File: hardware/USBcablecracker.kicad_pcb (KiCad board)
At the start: 2 copper layers, 100 x 50 mm, 57 parts, among them P1 USB_A, P10 USB_A, P11 USB_B, P12 CONN_01X09, P2 CONN_01X02, P3 USB_B-Micro, P6 CONN_01X09, P7 USB_B-Mini, P8 USB_B-Micro-3.0, P9 USB_TYPEC-S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

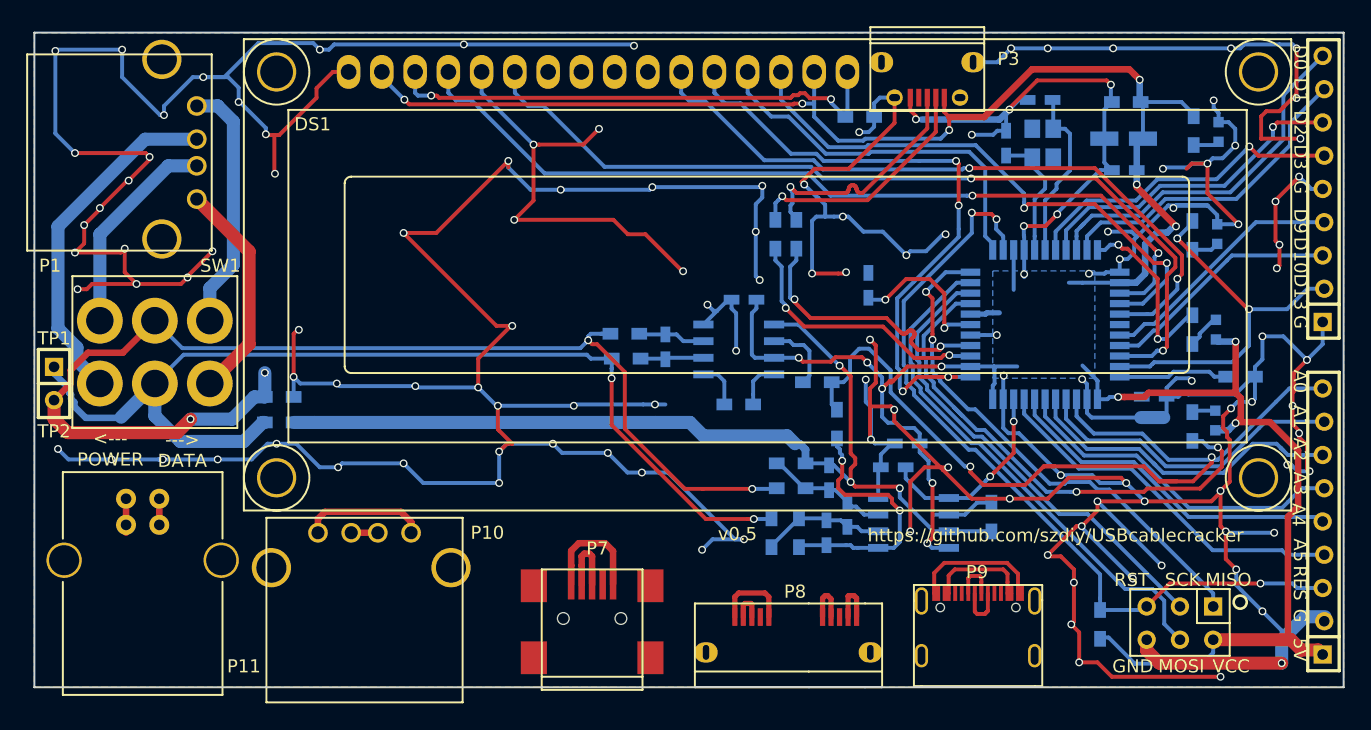
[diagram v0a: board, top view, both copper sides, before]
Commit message: Board cleanup first pass (still need to reconnect GND to U1)
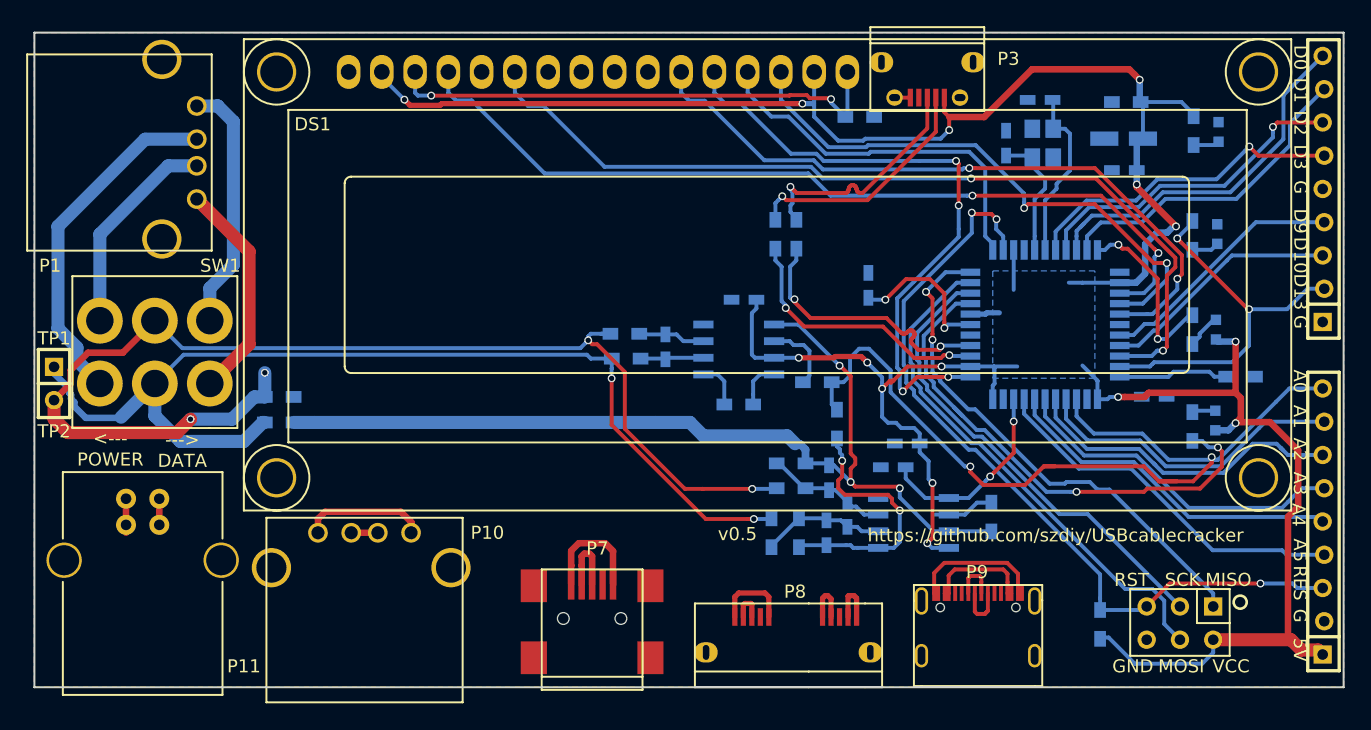
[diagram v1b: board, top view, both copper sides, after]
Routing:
- net GND: track 692.2 -> 1.20 mm, vias 128 -> 0
- net /D7: track 48.2 -> 47.6 mm

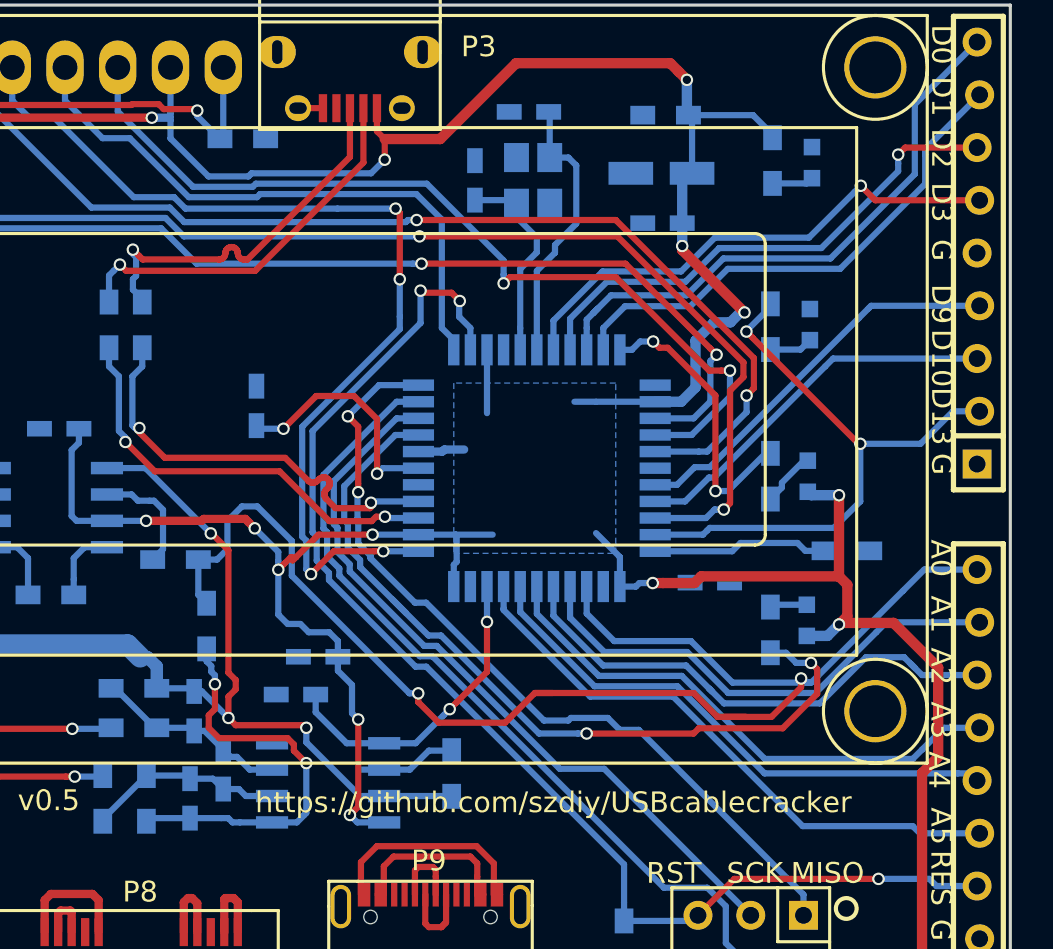
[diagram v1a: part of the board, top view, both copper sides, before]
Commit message: fixes net name (+5C to +5V), big hands -> big led pads
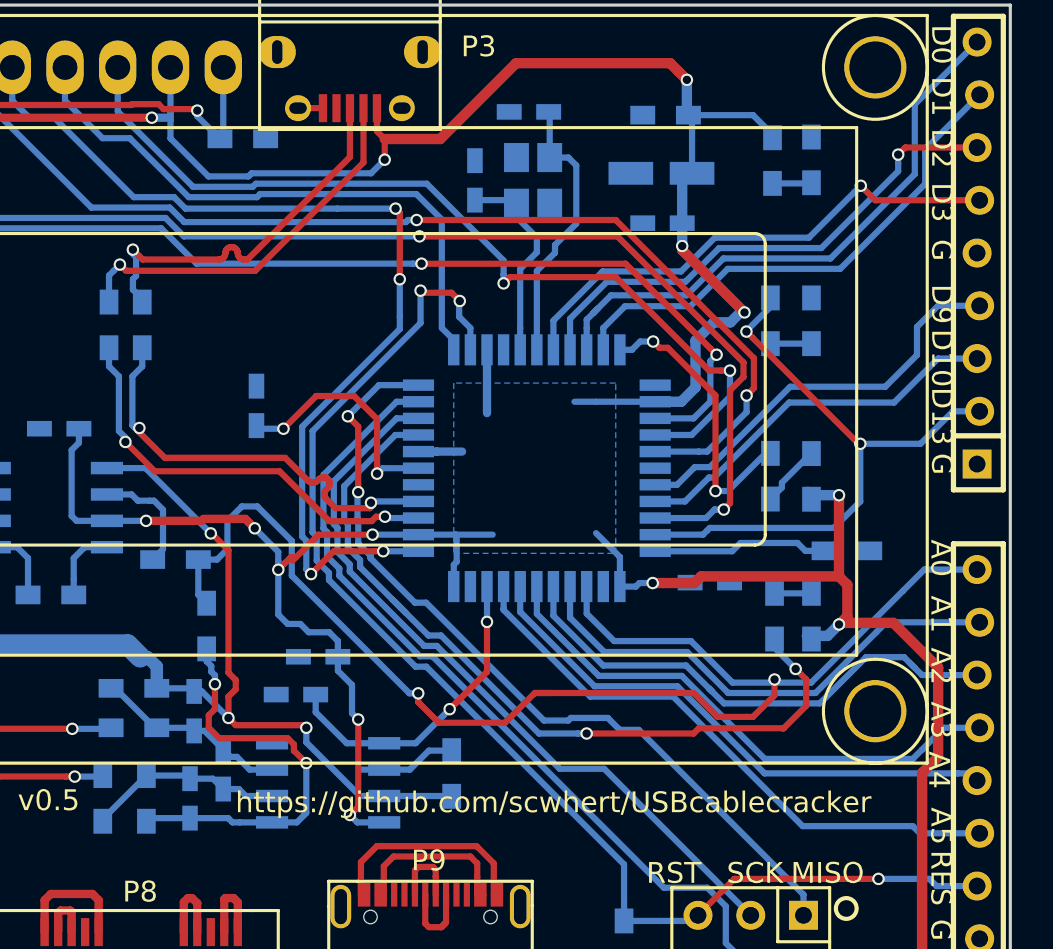
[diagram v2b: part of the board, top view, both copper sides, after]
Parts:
- D1, D2, D3, D4: footprint LEDs:LED_0603 -> LEDs:LED_0603_HandSoldering
- moved R2 0.69 mm to (138.6, 79.4)
- moved D1 0.30 mm to (140.4, 79.4)
- moved R4 0.28 mm to (138.4, 65.2)
- moved D3 0.20 mm to (140.4, 65.2)
- moved D2 0.18 mm to (140.4, 72.7)
- moved D4 0.13 mm to (140.4, 57.5)
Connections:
- net +5C renamed +5V
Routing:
- net /A0: track 67.2 -> 64.5 mm
- net /IO9: track 19.2 -> 20.0 mm
- net /RX_LED: track 39.6 -> 38.9 mm
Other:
- board text added: "https://github.com/scwhert/USBcablecracker"
- board text removed: "https://github.com/szdiy/USBcablecracker"

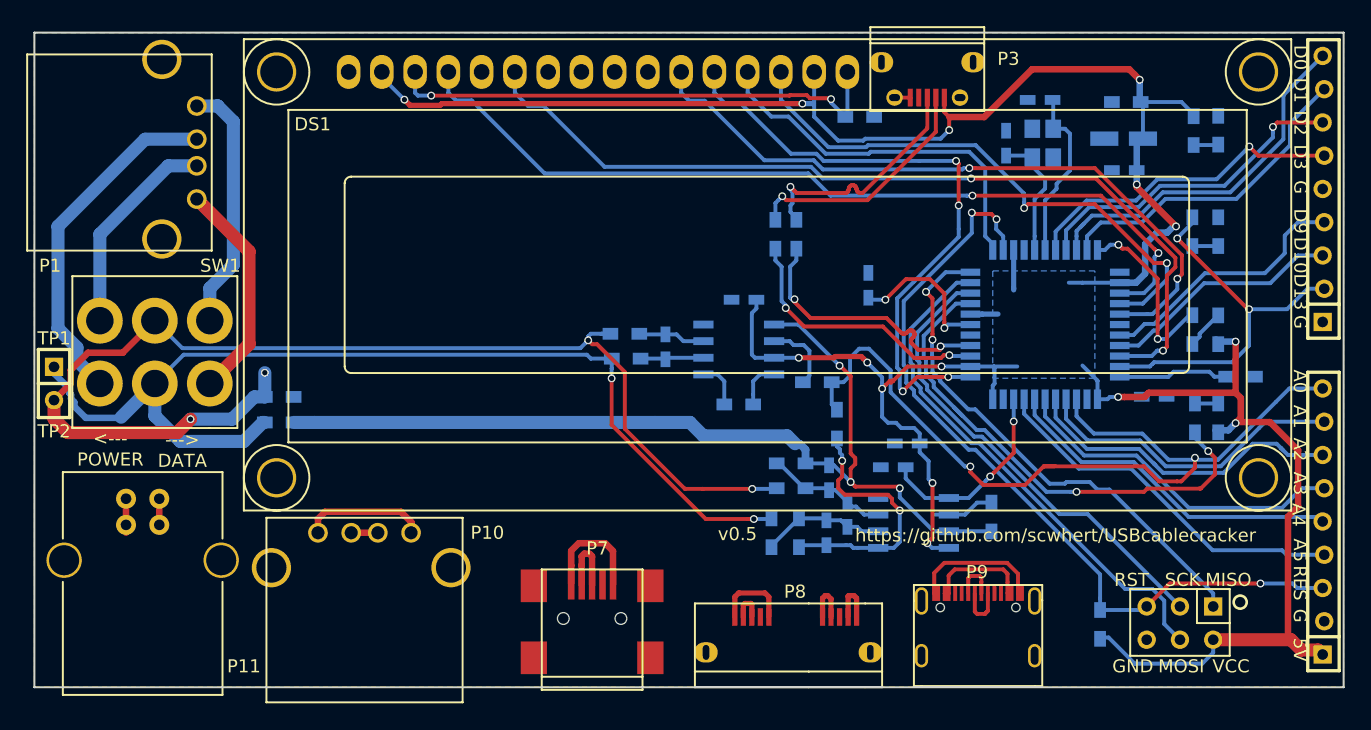
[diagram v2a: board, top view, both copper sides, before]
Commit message: no more GPIO breakout
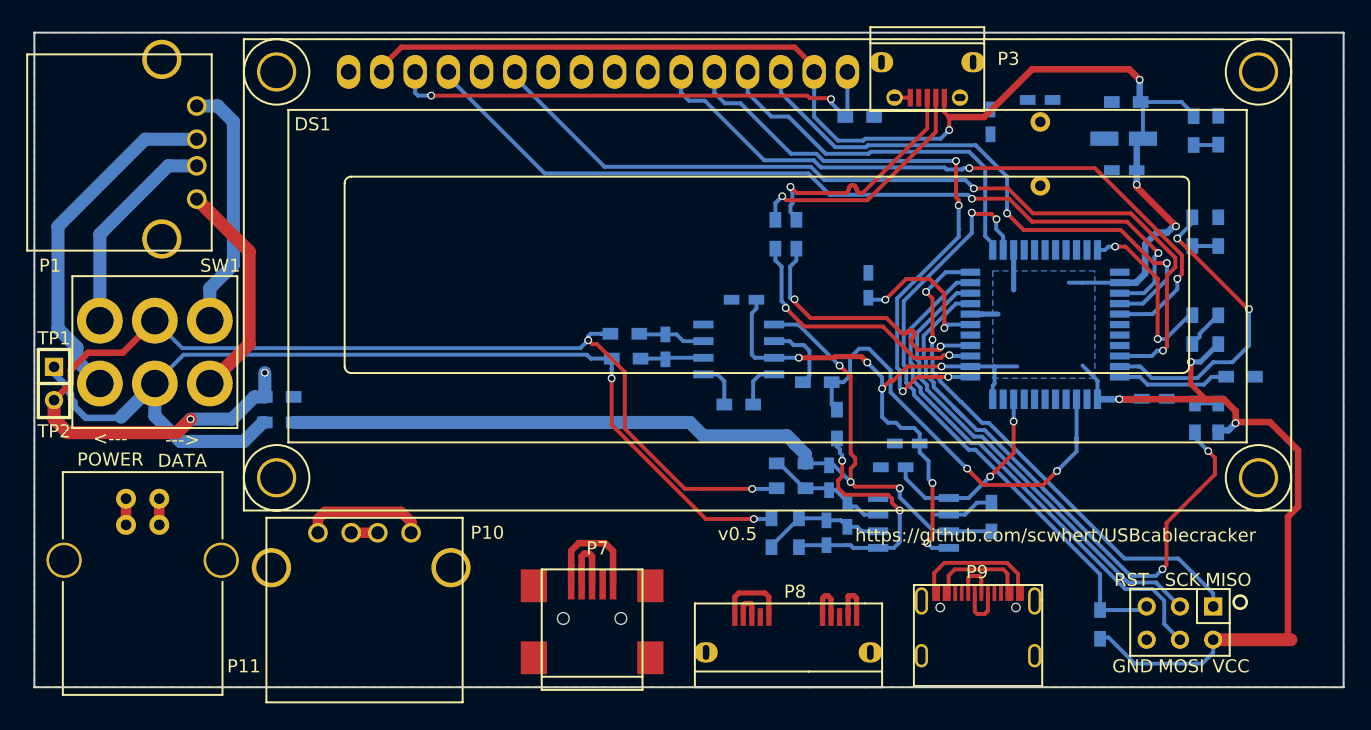
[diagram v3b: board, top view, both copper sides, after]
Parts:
- removed P12, P6: CONN_01X09, USBcablecracker:CONN_2.54mm_1x9
- Y1: footprint Crystals:crystal_FA238-TSX3225 -> Crystals:Crystal_HC49-U_Vertical
- moved C5 2.01 mm to (123.0, 56.8)
- moved Y1 1.63 mm to (126.8, 56.8)
- moved C12 0.16 mm to (135.5, 78.0)
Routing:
- net /A0: track 64.5 -> 34.0 mm
- net /A5: track 28.5 -> 0.00 mm
- net /D0: track 28.1 -> 0.00 mm
- net /A4: track 26.5 -> 0.00 mm
- net /A3: track 26.4 -> 0.00 mm
- net /A2: track 25.3 -> 0.00 mm
- net /D2: track 25.0 -> 0.00 mm, vias 1 -> 0
- net /D1: track 25.0 -> 0.00 mm
- net /D3: track 24.9 -> 0.00 mm, vias 1 -> 0
- net /A1: track 24.1 -> 0.00 mm
- net /IO9: track 20.0 -> 0.00 mm
- net /IO10: track 18.3 -> 0.00 mm
- net /RESET: track 61.7 -> 47.4 mm, vias 3 -> 2
- net /X+: track 13.3 -> 0.00 mm
- net /X-: track 9.86 -> 0.00 mm
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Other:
- board text removed: "5V"
- board text removed: "A0"
- board text removed: "A1"
- board text removed: "A2"
- board text removed: "A3"
- board text removed: "A4"
- board text removed: "A5"
- board text removed: "D0"
- board text removed: "D1"
- board text removed: "D10"
- board text removed: "D2"
- board text removed: "D3"
- board text removed: "D9"
- board text removed: "G"
- board text removed: "RES"

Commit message: crystal placement
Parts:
- removed U1: ATmega32U4-AU, Housings_QFP:TQFP-44_10x10mm_Pitch0.8mm
- moved D1 10.9 mm to (144.7, 89.5)
- moved R2 10.8 mm to (142.6, 89.5)
- moved Y1 6.47 mm to (131.5, 61.3), turned to 180 degrees
- moved C1 4.83 mm to (131.5, 56.2), turned to 90 degrees
- moved C8 4.57 mm to (137.8, 58.1)
- moved C9 4.57 mm to (137.8, 60.5)
- moved R9 4.57 mm to (138.0, 55.3)
- moved D4 4.32 mm to (144.7, 57.7)
- moved D2 4.32 mm to (144.7, 72.7)
- moved D3 4.32 mm to (144.7, 65.2)
- moved R3 4.14 mm to (142.6, 72.7)
- moved R4 4.14 mm to (142.6, 65.2)
- moved R5 4.04 mm to (142.6, 57.7)
- moved C5 3.61 mm to (126.6, 56.2)
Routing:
- net /X+: track 0.00 -> 11.3 mm
- net /X-: track 0.00 -> 9.60 mm
- net +5V: track 211.2 -> 219.7 mm, vias 13 -> 11
- net (no net): track 0.00 -> 6.71 mm, vias 0 -> 1
- net /RX_LED: track 46.7 -> 40.3 mm
- net /IO13: track 23.5 -> 18.1 mm, vias 2 -> 0
- net /A0: track 34.0 -> 37.1 mm
- net /TX_LED: track 13.7 -> 16.6 mm
- net /D6: track 53.0 -> 53.7 mm
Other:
- board text added: "V2.0"
- board text removed: "V1.0"
